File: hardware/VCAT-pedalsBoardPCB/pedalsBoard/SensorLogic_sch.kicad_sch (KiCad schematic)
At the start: 13 parts, among them U4 Opamp_Dual, U5 Opamp_Dual

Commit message: test
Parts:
- removed IRLML0030TRPBF: IRLML0030, SOT95P237X112-3N, symbol Transistor_FET:IRLML0030
- removed R11, R16: R, symbol Device:R
- removed R15: 10k, symbol Device:R
- added IRLML0030TRPBF1: IRLML0030, SOT95P237X112-3N, symbol Transistor_FET:IRLML0030
- added R20, R21, R39: 10k, Resistor_SMD:R_0603_1608Metric_Pad0.98x0.95mm_HandSolder, symbol Device:R
- added R37, R38: 5.1k, Resistor_SMD:R_0603_1608Metric_Pad0.98x0.95mm_HandSolder, symbol Device:R
- added TP10, TP12: TP_ACCPOT1_IN, symbol Connector:TestPoint
- added TP11: TP_ACCPOT2_OUT, symbol Connector:TestPoint
- added TP13: TP_BSWCH_IN, symbol Connector:TestPoint
- added TP14: TP_BSWCH_OUT, symbol Connector:TestPoint
- added TP15: TP_BSENS2_OUT, symbol Connector:TestPoint
- added TP16: TP_BSENS1_OUT, symbol Connector:TestPoint
- added TP17: TP_BSENS_IN, symbol Connector:TestPoint
- added TP9: TP_ACCPOT2_IN, symbol Connector:TestPoint
- C22, C24: value C -> .1uF; footprint (none) -> Capacitor_SMD:C_0603_1608Metric_Pad1.08x0.95mm_HandSolder
- C23, C25: value C -> 10uF; footprint (none) -> Capacitor_SMD:C_0603_1608Metric_Pad1.08x0.95mm_HandSolder
- R14: footprint (none) -> Resistor_SMD:R_0603_1608Metric_Pad0.98x0.95mm_HandSolder
- R17: value R -> 10k; footprint (none) -> Resistor_SMD:R_0603_1608Metric_Pad0.98x0.95mm_HandSolder
- R18: value R -> 5.1k; footprint (none) -> Resistor_SMD:R_0603_1608Metric_Pad0.98x0.95mm_HandSolder
- U4: footprint (none) -> MyParts:SOIC127P600X175-8N
- U5: footprint SOIC127P600X175-8N -> MyParts:SOIC127P600X175-8N
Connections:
- net 3.3V: now also R21.1
- net ACCEL2_OUT: now also R38.2
- net B_SENS: now also R37.2; no longer U4.3 (+), U4.5 (+)
- net B_SENSOUT1: now also TP16.1
- net B_SENSOUT2: now also TP15.1
- net B_SWCH_OUT: now also IRLML0030TRPBF1.3 (D), R21.2, TP14.1
- net B_SWITCH: now also IRLML0030TRPBF1.1 (G), R20.1, TP13.1; no longer R14.1
- net GND: now also R14.1, IRLML0030TRPBF1.2 (S), R20.2, R39.1; no longer R14.2
- net at R17.2, R18.1, U5.5 (+): now also TP9.1
- net at U5.3 (+): now also R38.1, R39.2, TP10.1
- net ACCPOT_ADC_1 renamed ACCPOT_1
- net ACCPOT_1: now also TP12.1
- net ACCPOT_ADC_2 renamed ACCPOT_2
- net ACCPOT_2: now also TP11.1
- new net: R14.2, R37.1, TP17.1, U4.3 (+), U4.5 (+)
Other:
- note removed: "Potentiometer Buffering and Output"
- note removed: "Unity Gain Buffer Power"
- moved on the sheet: C22, C23, C24, C25, R17, R18, U4A, U4B, U4C, U5A, U5B, U5C

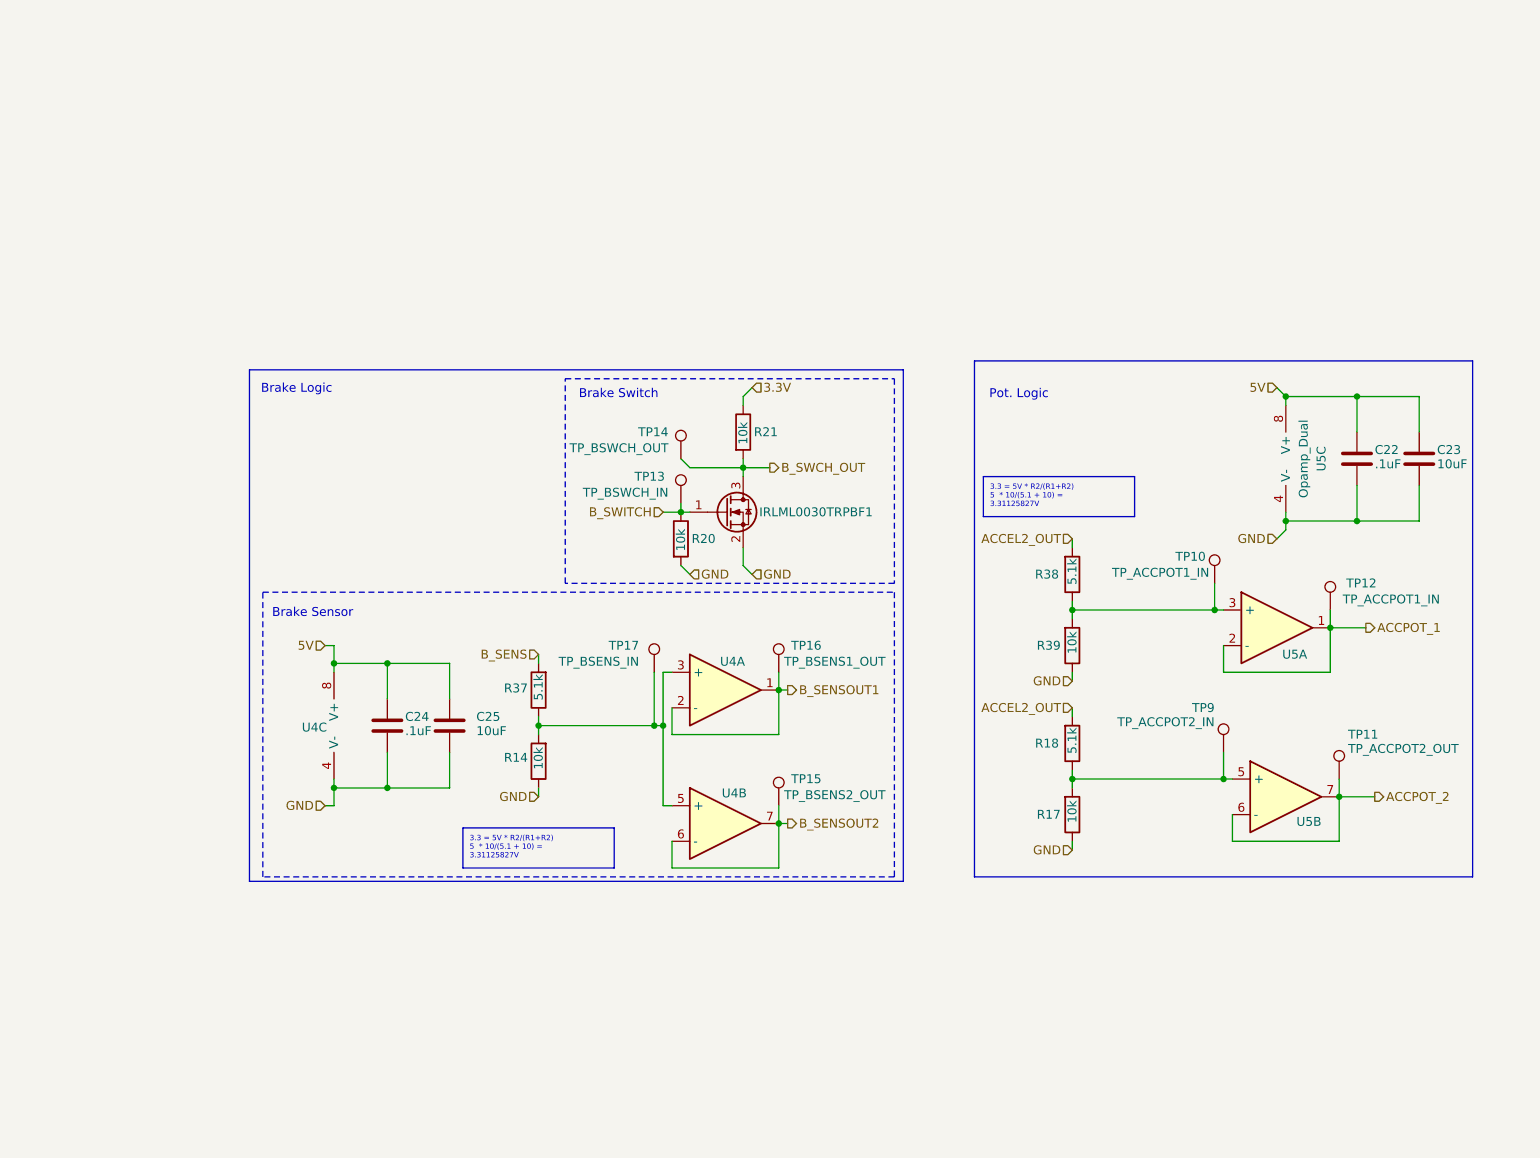
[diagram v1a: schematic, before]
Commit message: implemented review suggestions and added bus
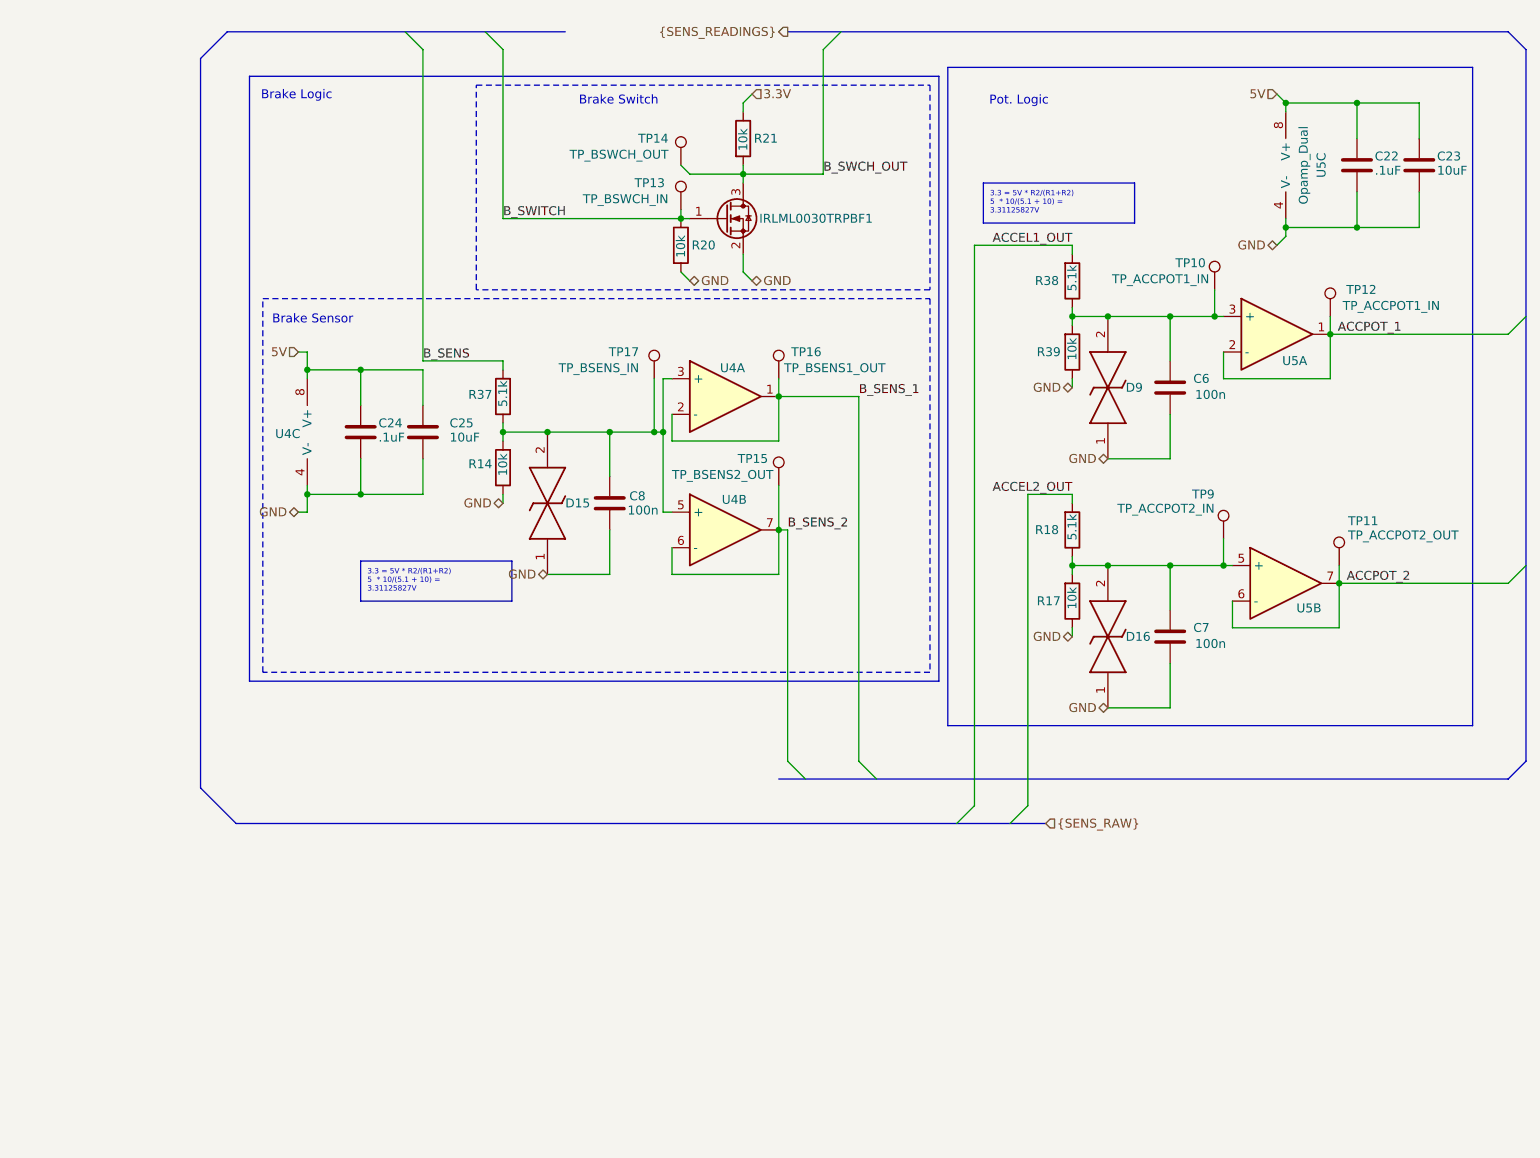
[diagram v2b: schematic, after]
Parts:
- added C6, C7, C8: 100n, SD15C01FTG, symbol Device:C
- added D15, D16, D9: SD15C-01FTG, MyParts:SD15C01FTG, symbol SD15C-01FTG:SD15C-01FTG
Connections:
- net ACCEL2_OUT: no longer R38.2
- net GND: now also C6.2, C7.2, C8.2, D15.1, D16.1, D9.1
- net at R14.2, R37.1, TP17.1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: now also C8.1, D15.2
- net at R17.2, R18.1, TP9.1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: now also C7.1, D16.2
- net at R38.1, R39.2, TP10.1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: now also C6.1, D9.2
- net B_SENSOUT1 renamed B_SENS_1
- net B_SENSOUT2 renamed B_SENS_2
- new net ACCEL1_OUT: R38.2
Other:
- moved on the sheet: C22, C23, C24, C25, IRLML0030TRPBF1, R14, R17, R18, R20, R21, R37, R38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

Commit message: addressed review, brake switch on slack
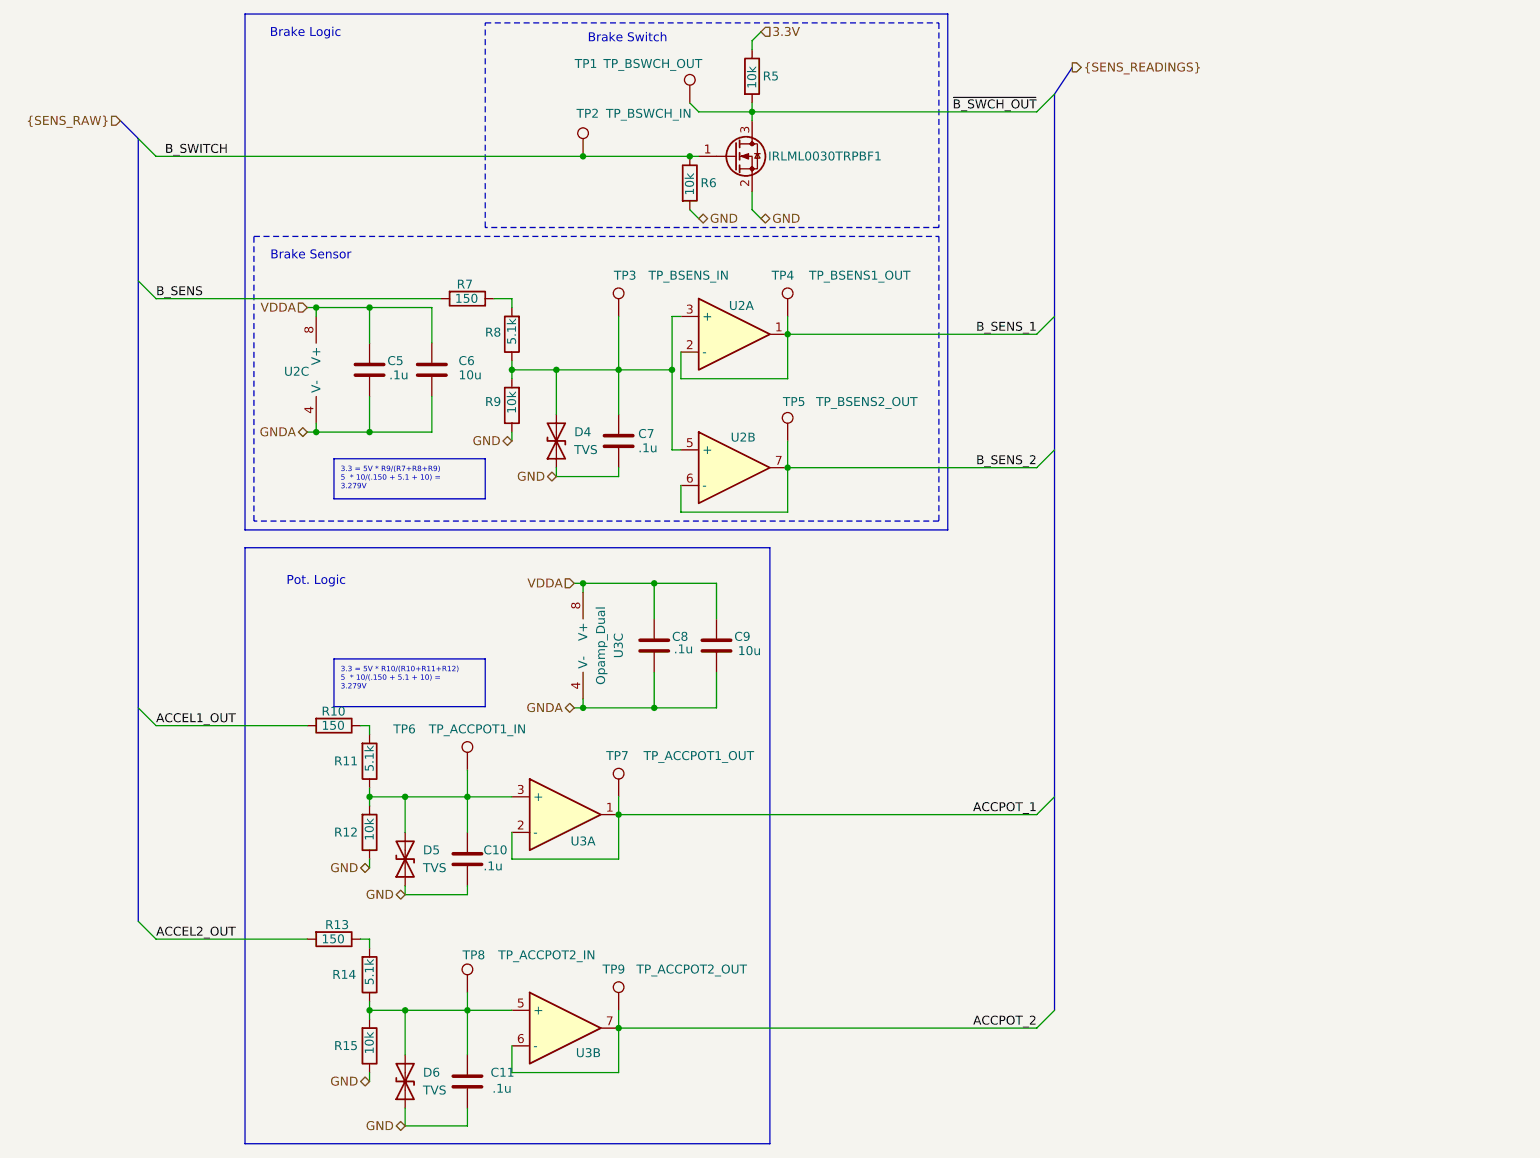
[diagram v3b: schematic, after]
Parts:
- removed D15, D16, D9: SD15C-01FTG, MyParts:SD15C01FTG, symbol SD15C-01FTG:SD15C-01FTG
- removed TP10, TP12: TP_ACCPOT1_IN, symbol Connector:TestPoint
- removed TP11: TP_ACCPOT2_OUT, symbol Connector:TestPoint
- removed TP13: TP_BSWCH_IN, symbol Connector:TestPoint
- removed TP14: TP_BSWCH_OUT, symbol Connector:TestPoint
- removed TP15: TP_BSENS2_OUT, symbol Connector:TestPoint
- removed TP16: TP_BSENS1_OUT, symbol Connector:TestPoint
- removed TP17: TP_BSENS_IN, symbol Connector:TestPoint
- added D4, D5, D6: TVS, MyParts:SD15C01FTG, symbol lhrs_misc:Boot_TVS
- added R10, R13, R7: 150, Resistor_SMD:R_0603_1608Metric_Pad0.98x0.95mm_HandSolder, symbol Device:R
- added TP1: TP_BSWCH_OUT, symbol Connector:TestPoint
- added TP2: TP_BSWCH_IN, symbol Connector:TestPoint
- added TP3: TP_BSENS_IN, symbol Connector:TestPoint
- added TP4: TP_BSENS1_OUT, symbol Connector:TestPoint
- added TP5: TP_BSENS2_OUT, symbol Connector:TestPoint
- added TP6: TP_ACCPOT1_IN, symbol Connector:TestPoint
- added TP7: TP_ACCPOT1_OUT, symbol Connector:TestPoint
- added TP8: TP_ACCPOT2_IN, symbol Connector:TestPoint
- C10: renamed from C6; value 100n -> .1u
- C11: renamed from C7; value 100n -> .1u
- C5: renamed from C24; value .1uF -> .1u
- C6: renamed from C25; value 10uF -> 10u
- C7: renamed from C8; value 100n -> .1u
- C8: renamed from C22; value .1uF -> .1u
- C9: renamed from C23; value 10uF -> 10u
- TP9: value TP_ACCPOT2_IN -> TP_ACCPOT2_OUT
- renumbered R38 to R11, R39 to R12, R18 to R14, R17 to R15, R21 to R5, R20 to R6, R37 to R8, R14 to R9, U4 to U2, U5 to U3
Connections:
- net ACCEL1_OUT: now also R10.2; no longer R11.2
- net ACCEL2_OUT: now also R13.2; no longer R14.2
- net ACCPOT_1: now also TP7.1
- net ACCPOT_2: now also TP9.1
- net B_SENS: now also R7.2; no longer R8.2
- net B_SENS_1: now also TP4.1
- net B_SENS_2: now also TP5.1
- net B_SWITCH: now also TP2.1
- net GND: now also D4.1 (A1), D5.1 (A1), D6.1 (A1); no longer C5.1, C6.1, C8.1, C9.1, U2.4 (V-), U3.4 (V-)
- net at C7.1, R8.1, R9.2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: now also D4.2 (A2), TP3.1
- net at C10.1, R11.1, R12.2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: now also D5.2 (A2), TP6.1
- net at C11.1, R14.1, R15.2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: now also D6.2 (A2), TP8.1; no longer TP9.1
- net 5V renamed VDDA
- net B_SWCH_OUT renamed ~{B_SWCH_OUT}
- net ~{B_SWCH_OUT}: now also TP1.1
- new net: R13.1, R14.2
- new net: R7.1, R8.2
- new net: R10.1, R11.2
- new net GNDA: C5.1, C6.1, C8.1, C9.1, U2.4 (V-), U3.4 (V-)
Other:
- moved on the sheet: C10, C11, C5, C6, C7, C8, C9, IRLML0030TRPBF1, R11, R12, R14, R15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

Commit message: hopefully final before layout
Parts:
- removed IRLML0030TRPBF1: IRLML0030, SOT95P237X112-3N, symbol Transistor_FET:IRLML0030
- removed R5, R6: 10k, Resistor_SMD:R_0603_1608Metric_Pad0.98x0.95mm_HandSolder, symbol Device:R
- removed TP1: TP_BSWCH_OUT, symbol Connector:TestPoint
- removed TP2: TP_BSWCH_IN, symbol Connector:TestPoint
- C10, C11, C7: footprint SD15C01FTG -> Capacitor_SMD:C_0603_1608Metric_Pad1.08x0.95mm_HandSolder
- D4, D5, D6: footprint MyParts:SD15C01FTG -> Diode_SMD:D_SOD-323
- TP3, TP4, TP5, TP6, TP7, TP8, TP9: footprint (none) -> LHRS_Special:TestPoint_HEX_3mmID
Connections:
- net RAW_ACCEL1: now reaches C10.1, D5.2 (A2), R11.1, R12.2, TP6.1, U3.3 (+)
- net RAW_BSENS: now reaches D4.2 (A2), R8.1, R9.2, U2.3 (+), U2.5 (+)
- net RAW_BSENS: no longer C7.1, TP3.1
- net RAW_ACCEL2: now reaches C11.1, D6.2 (A2), R14.1, R15.2, TP8.1, U3.5 (+)
- new net: C7.1, TP3.1
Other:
- note removed: "Brake Sensor"
- note removed: "Brake Switch"
- moved on the sheet: TP4, TP5, TP6, TP8, U2A, U2B
